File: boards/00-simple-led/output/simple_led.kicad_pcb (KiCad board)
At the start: 2 copper layers, 25 x 20 mm, 3 parts, among them J1 PWR

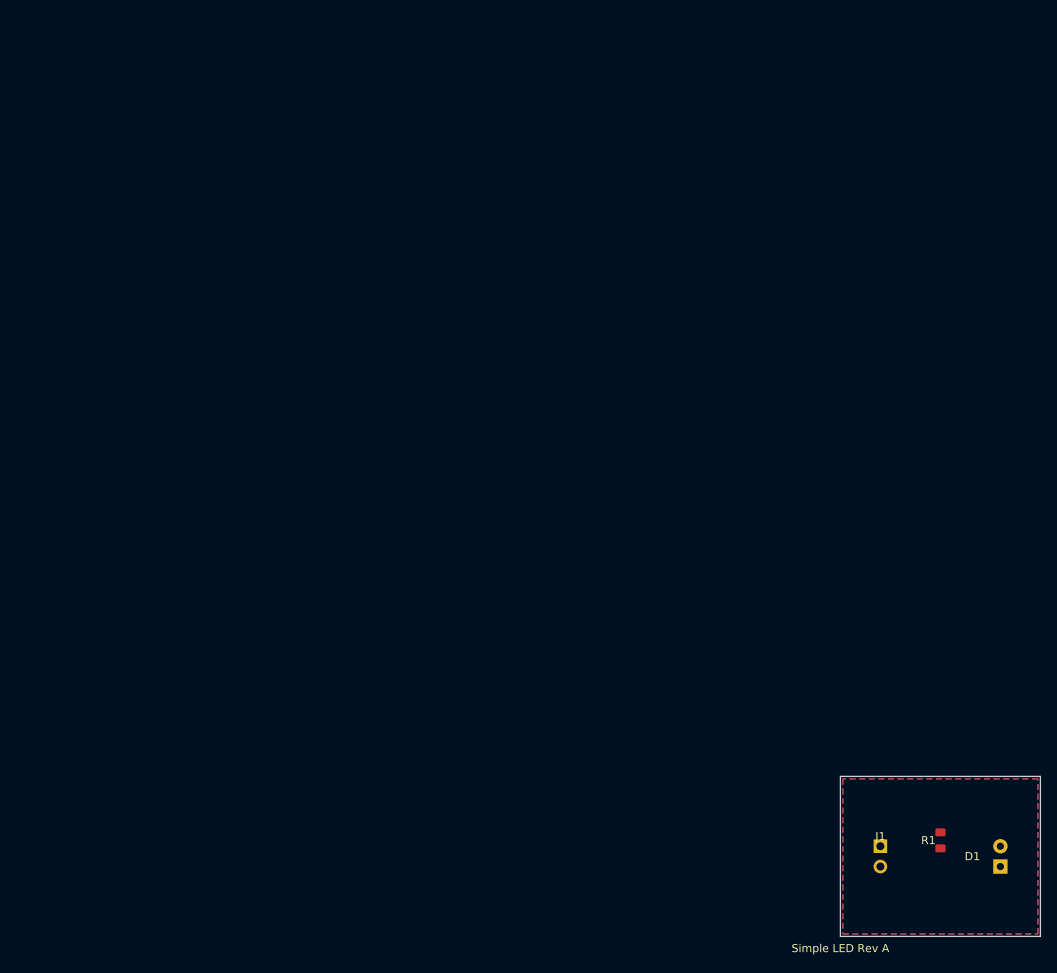
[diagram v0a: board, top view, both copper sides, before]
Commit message: feat(pcb): add page_fit to size sheet to board + center, apply to all boards
Add PCB.page_fit(margin=5.0) which rewrites the (paper ...) node to a tight
(paper "User" W H) sized to the Edge.Cuts bbox plus a uniform margin and
translates every board item (footprints, segments, vias, zones incl.
filled_polygons, gr_* graphics, text) so the board is centered with that
margin. Pure geometric translate — relative geometry, routing and DRC
validity are preserved, no re-route needed.

Expose it as `kct pcb page-fit <pcb> [-o out] [--margin] [--dry-run]` and
wire a PAGE_FIT build step (after stitch, before verify/export) so future
boards are centered too. Apply page_fit to all demo boards (00-07 +
external/softstart), both routed and unrouted PCBs, so the committed
layouts fill + center the KiCanvas viewer instead of sitting tiny in an A4
page. Boards 00/01 stay DRC-clean (0 errors); no board's DRC count changed.

Co-Authored-By: Claude Opus 4.7 <noreply@anthropic.com>
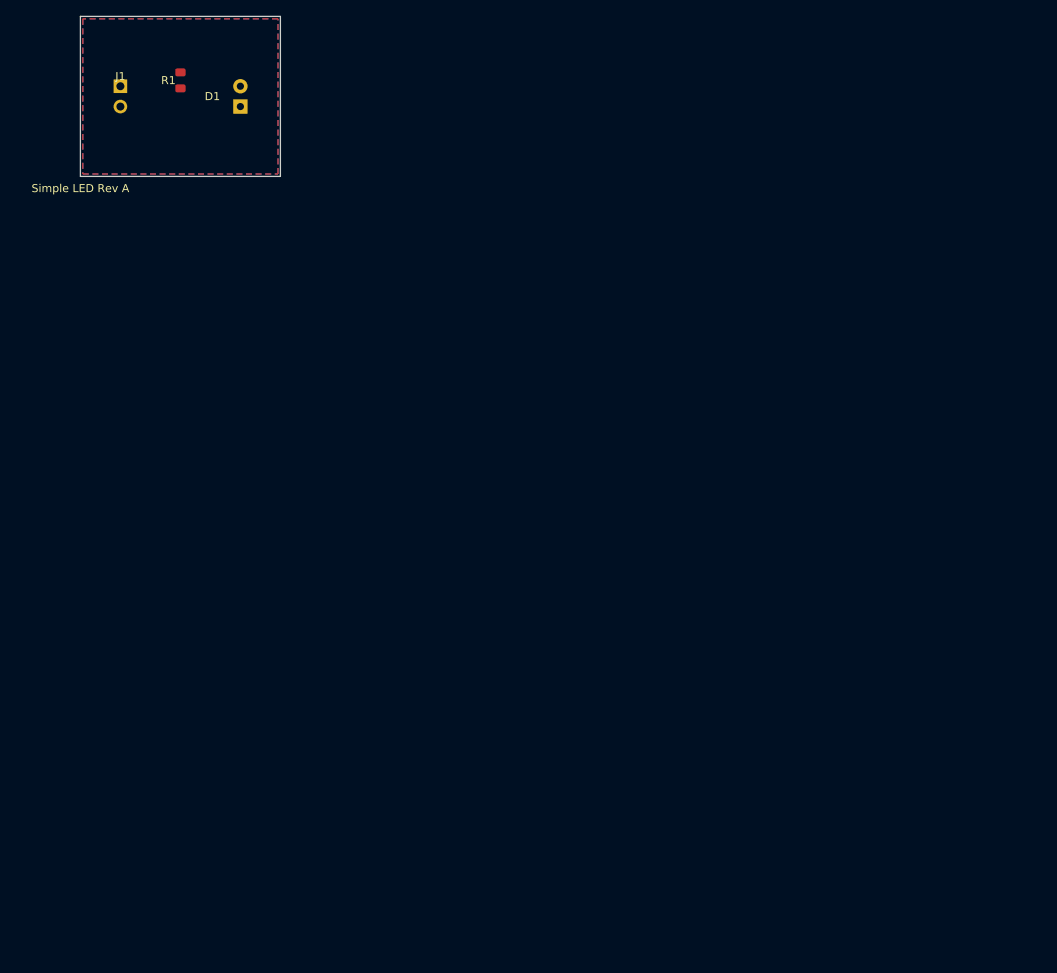
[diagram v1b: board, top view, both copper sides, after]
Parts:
- moved D1 134.4 mm to (25.0, 15.0)
- moved J1 134.4 mm to (10.0, 15.0)
- moved R1 134.4 mm to (17.5, 13.0)
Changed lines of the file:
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@@
 (kicad_pcb
 	(version 20240108)
+	(paper "User" 35 30)
 	(generator "kicad-tools-demo")
 	(generator_version "9.0")
@@
 		(legacy_teardrops no)
 	)
-	(paper "A4")
 	(layers
 		(0 "F.Cu" signal)
@@
 	(net 3 "GND")
 	(gr_rect
-		(start 100.0 100.0)
-		(end 125.0 120.0)
+		(start 5 5)
+		(end 30 25)
 		(stroke
 			(width 0.1)
@@
 	(footprint "Connector_PinHeader_2.54mm:PinHeader_1x02_P2.54mm_Vertical"
 		(layer "F.Cu")
-		(at 105.0 110.0)
+		(at 10 15)
 		(fp_text reference "J1"
 			(at 0 -2.5)
@@
 	(footprint "Resistor_SMD:R_0805_2012Metric"
 		(layer "F.Cu")
-		(at 112.5 108.0 90)
+		(at 17.5 13 90)
 		(fp_text reference "R1"
 			(at 0 -1.5)
@@
 	(footprint "LED_THT:LED_D5.0mm"
 		(layer "F.Cu")
-		(at 120.0 110.0 90)
+		(at 25 15 90)
 		(fp_text reference "D1"
 			(at 0 -3.5)
@@
 		(fill yes (thermal_gap 0.3) (thermal_bridge_width 0.4)
 		)
-		(polygon (pts (xy 100.3 100.3) (xy 100.3 119.7) (xy 124.7 119.7) (xy 124.7 100.3))
+		(polygon (pts (xy 5.3 5.3) (xy 5.3 24.7) (xy 29.7 24.7) (xy 29.7 5.3))
 		)
 	)
@@
 		(fill yes (thermal_gap 0.3) (thermal_bridge_width 0.4)
 		)
-		(polygon (pts (xy 100.3 100.3) (xy 100.3 119.7) (xy 124.7 119.7) (xy 124.7 100.3))
+		(polygon (pts (xy 5.3 5.3) (xy 5.3 24.7) (xy 29.7 24.7) (xy 29.7 5.3))
 		)
 	)
 	(gr_text "Simple LED Rev A"
-		(at 100 121.5)
+		(at 5 26.5)
 		(layer "F.SilkS")
 		(effects

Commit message: fix(pcb): page-fit routed boards only; revert unrouted sources (refs #3714)
page_fit was applied to and committed for the UNROUTED board sources too.
Because the autorouter is absolute-grid-position-dependent, translating the
unrouted boards changed routing outcomes and turned CI red on three jobs:
- Test: board-02 re-route produced a platform-specific segment count.
- Diff-Pair (06) / Match-Group (07): re-routing the moved unrouted boards
  fractured plane nets under the copper-union pour audit (#3509/#3617).

page_fit is a pure post-route translation, so it must touch the ROUTED
output only:
- Revert every unrouted boards/*/output/<name>.kicad_pcb to origin/main
  (byte-identical); keep the page-fitted *_routed.kicad_pcb (gallery/viewer).
- Revert tests/router/test_board02_manufacturable_baseline.py to main
  (unrouted board-02 unchanged -> reproduces main's result).
- Build hook: _run_step_page_fit now operates on the routed PCB only and
  skips cleanly when no routed output exists, instead of falling back to and
  persisting a page-fit unrouted PCB.

Retains the sound geometry fixes (translation-invariant
point_to_segment_distance, _format_coord_mm, diffpair +1e-6 window tolerance).

Co-Authored-By: Claude Opus 4.7 <noreply@anthropic.com>
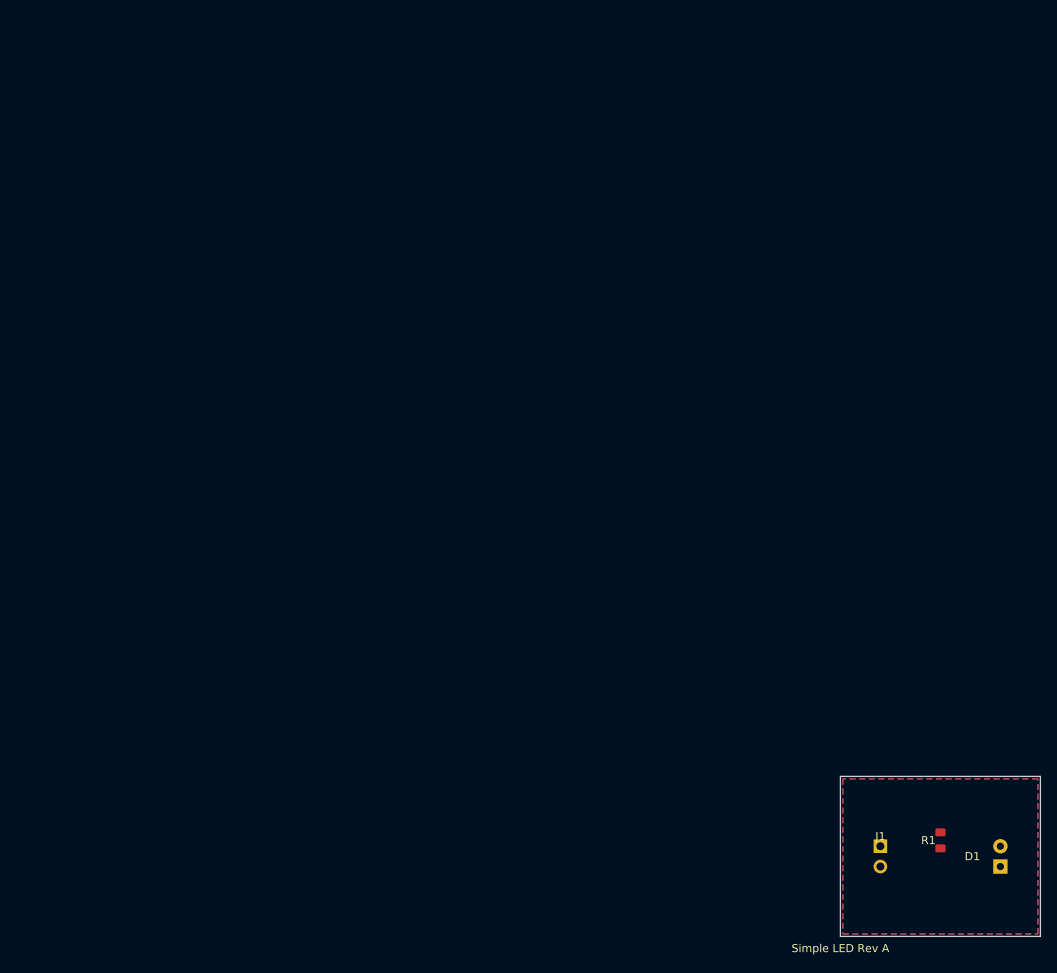
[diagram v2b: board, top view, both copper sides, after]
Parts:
- moved D1 134.4 mm to (120.0, 110.0)
- moved J1 134.4 mm to (105.0, 110.0)
- moved R1 134.4 mm to (112.5, 108.0)
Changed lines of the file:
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@@
 (kicad_pcb
 	(version 20240108)
-	(paper "User" 35 30)
 	(generator "kicad-tools-demo")
 	(generator_version "9.0")
@@
 		(legacy_teardrops no)
 	)
+	(paper "A4")
 	(layers
 		(0 "F.Cu" signal)
@@
 	(net 3 "GND")
 	(gr_rect
-		(start 5 5)
-		(end 30 25)
+		(start 100.0 100.0)
+		(end 125.0 120.0)
 		(stroke
 			(width 0.1)
@@
 	(footprint "Connector_PinHeader_2.54mm:PinHeader_1x02_P2.54mm_Vertical"
 		(layer "F.Cu")
-		(at 10 15)
+		(at 105.0 110.0)
 		(fp_text reference "J1"
 			(at 0 -2.5)
@@
 	(footprint "Resistor_SMD:R_0805_2012Metric"
 		(layer "F.Cu")
-		(at 17.5 13 90)
+		(at 112.5 108.0 90)
 		(fp_text reference "R1"
 			(at 0 -1.5)
@@
 	(footprint "LED_THT:LED_D5.0mm"
 		(layer "F.Cu")
-		(at 25 15 90)
+		(at 120.0 110.0 90)
 		(fp_text reference "D1"
 			(at 0 -3.5)
@@
 		(fill yes (thermal_gap 0.3) (thermal_bridge_width 0.4)
 		)
-		(polygon (pts (xy 5.3 5.3) (xy 5.3 24.7) (xy 29.7 24.7) (xy 29.7 5.3))
+		(polygon (pts (xy 100.3 100.3) (xy 100.3 119.7) (xy 124.7 119.7) (xy 124.7 100.3))
 		)
 	)
@@
 		(fill yes (thermal_gap 0.3) (thermal_bridge_width 0.4)
 		)
-		(polygon (pts (xy 5.3 5.3) (xy 5.3 24.7) (xy 29.7 24.7) (xy 29.7 5.3))
+		(polygon (pts (xy 100.3 100.3) (xy 100.3 119.7) (xy 124.7 119.7) (xy 124.7 100.3))
 		)
 	)
 	(gr_text "Simple LED Rev A"
-		(at 5 26.5)
+		(at 100 121.5)
 		(layer "F.SilkS")
 		(effects

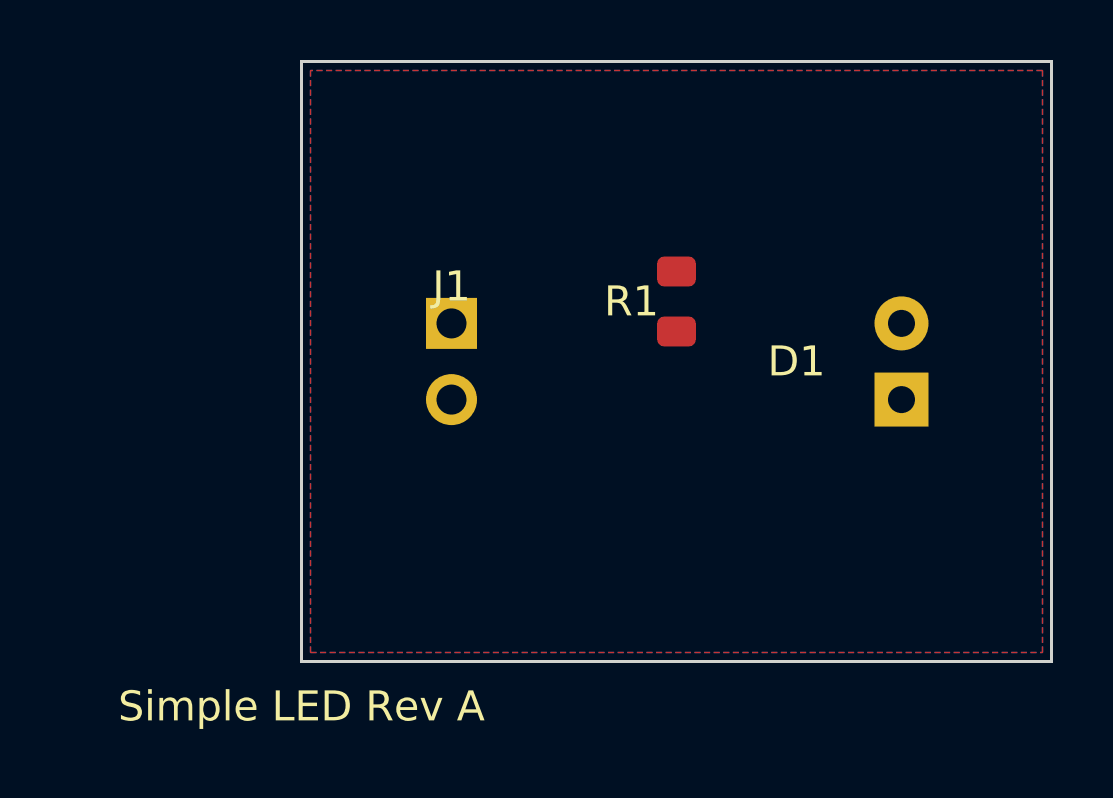
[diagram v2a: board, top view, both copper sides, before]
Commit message: fix(board-00): rotation-0 footprints + deterministic LED_ANODE route for 0 DRC under both engines (#3738)
* fix(board-00): rotation-0 footprints + deterministic LED_ANODE route → 0 DRC under both engines

Board 00 (simple-led) shipped genuine copper shorts under kicad-cli
(GND↔LED_ANODE, LED_ANODE↔VCC, plus the matching front solder-mask
bridges). Root cause: R1 and D1 were placed at a 90° rotation, and
kicad-tools' internal pad-position transform (kct check, the autorouter,
zone fill) models KiCad's on-disk footprint angle as a counter-clockwise
math rotation, whereas KiCad applies it clockwise in its Y-down frame.
For cardinal 90°/270° rotations the two conventions place pin 1 vs pin 2
at mirror-image positions, so the autorouter wired LED_ANODE to R1's VCC
pad and D1's GND pad (a real short kicad-cli flagged) while kct check —
using the same mirrored convention as the router — saw it as "correct".
No single routing could satisfy both engines.

Fix (board-local, no shared-code change):
- Place every footprint at rotation 0, where sin(angle)=0 and both
  conventions agree on pad positions. Board 00 was the only demo board
  using a 90° rotation, so this removes the ambiguity without affecting
  any other board (all others already use 0°).
- Replace the grid autorouter's LED_ANODE result (which still grazed D1's
  GND pad) with a deterministic L-shaped route derived from the actual
  pad positions, clearing the foreign GND pad with margin.

Result: kicad-cli DRC 0 shorts / 0 solder_mask_bridge / 0 unconnected /
0 isolated_copper; kct check --mfr jlcpcb --errors-only = 0; CI strict
routed-DRC gate = 0; report.md DRC Status = PASS. Manufacturing bundle
regenerated with --mfr jlcpcb-tier1.

Closes #3737

Co-Authored-By: Claude Opus 4.7 <noreply@anthropic.com>

* fix(board-00): true-45 LED_ANODE knee so the descent clears the 45° census gate

The GND-clearance guard in _rewrite_led_anode_route() nudged the knee to
(d1_gnd_x + 1.5, ...), giving the descent leg unequal dx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
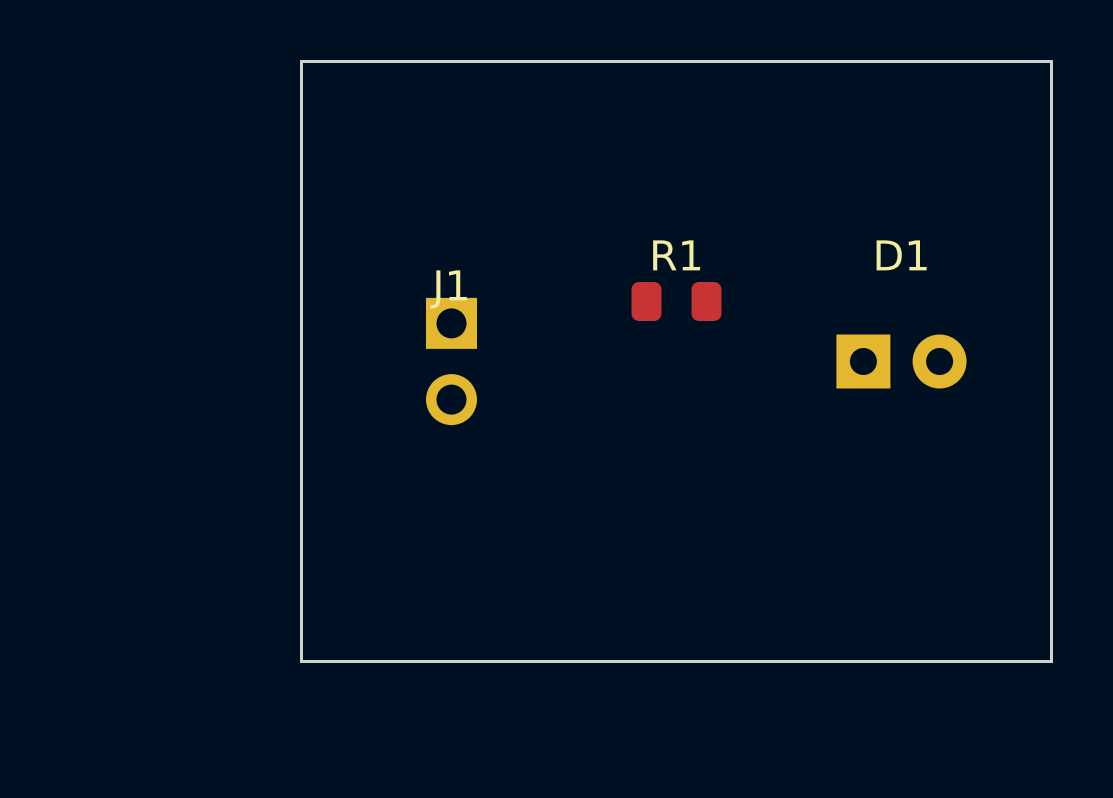
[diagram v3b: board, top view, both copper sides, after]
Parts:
- turned D1 to 0 degrees
- turned R1 to 0 degrees
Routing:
- removed copper zone on B.Cu, net GND
- removed copper zone on F.Cu, net VCC
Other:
- board text removed: "Simple LED Rev A"

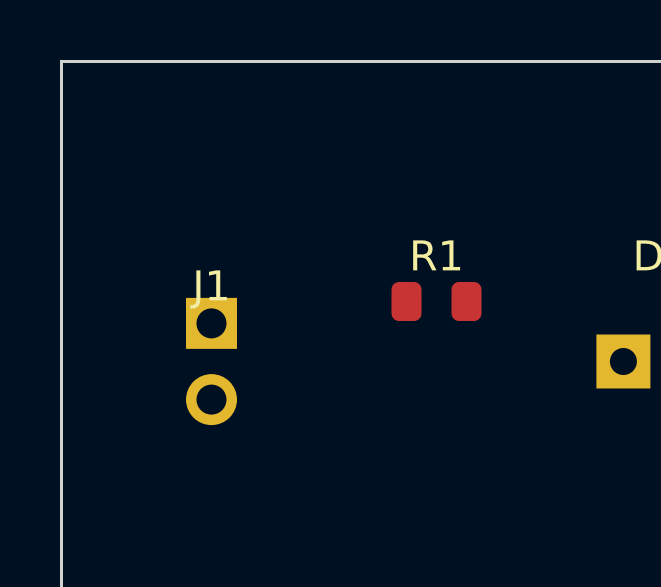
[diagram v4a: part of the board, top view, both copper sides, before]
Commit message: fix(boards): move connector refdes off pad-1 copper on boards 00/01 (#3962)
* fix(boards): move connector refdes off pad-1 copper on boards 00/01

The demo-board PCB generators for boards 00 (simple-led) and 01
(voltage-divider) hard-coded the connector refdes at local (0, -2.5),
placing the reference-designator text box over pad 1's exposed mask
aperture. Pad 1 is a 1.7x1.7 mm thru-hole centred at (0, -1.27), so its
copper top edge is at -2.12 mm; a 1x1 mm / 0.15 mm-stroke refdes has its
bottom edge 0.575 mm below centre, so -2.5 left the box inside the
aperture and fired silk_over_copper on J1/J2.

Move the connector refdes to (0, -3.5) -- the same offset the LED
footprint already uses and passes silk_over_copper -- which clears the
aperture with margin. Add a geometry-based justification in each
generate_connector docstring. The resistor refdes at (0, -1.5) was
already clear of the 0805 pads and is unchanged.

Regenerate boards 00 and 01 committed artifacts from the fixed
generators. Fresh kct check and kicad-cli pcb drc --refill-zones both
report 0 silk_over_copper (and 0 total DRC violations) on the routed
PCBs.

Remove the _SILK_PLACEMENT_RULES carve-out from
tests/test_board_01_ship_ready.py so the strict 0-warning gate holds
unconditionally, and move board 01 from the silk_over_copper positive
fixture to the clean-board list in tests/test_validate_silkscreen.py.

Closes #3939

Co-Authored-By: Claude Fable 5 <noreply@anthropic.com>

* fix(board-01): restore #3715 page-fit on regenerated routed artifact

The generator-only regen dropped the PAGE_FIT post-pass that produced
main's committed truth, reverting (paper "User" 40 35) -> (paper "A4")
and un-centering the board from ~10-30mm back to a full-A4 ~105-125mm
layout, silently undoing the #3715 gallery-centering.

Re-ran the routed artifact through the same pipeline main uses:
`kct pcb page-fit --margin 5.0` after routing, then regenerated the
JLCPCB manufacturing bundle from the page-fit board.

Verification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
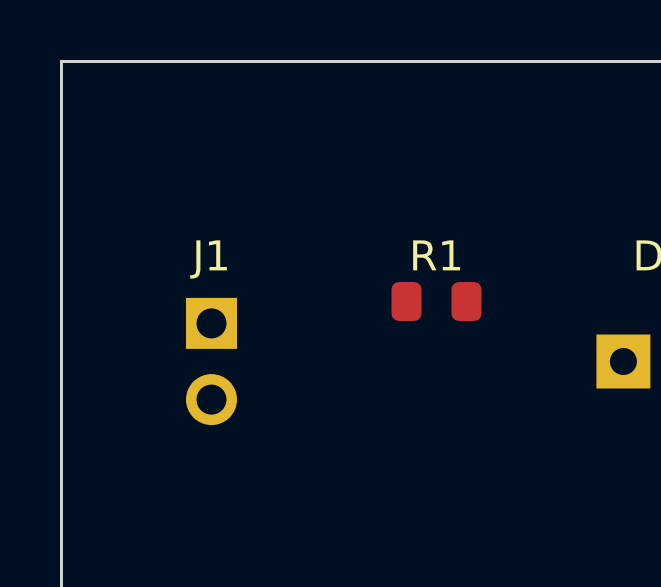
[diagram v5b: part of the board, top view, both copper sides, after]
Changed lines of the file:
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@@
     (layer "F.Cu")
     (at 105.0 110.0)
-    (fp_text reference "J1" (at 0 -2.5) (layer "F.SilkS")
+    (fp_text reference "J1" (at 0 -3.5) (layer "F.SilkS")
       (effects (font (size 1 1) (thickness 0.15)))
     )
